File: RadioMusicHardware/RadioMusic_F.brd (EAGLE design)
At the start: 107 x 19.5 mm, 31 parts, among them X1 VERT_SD_CARD_REV2

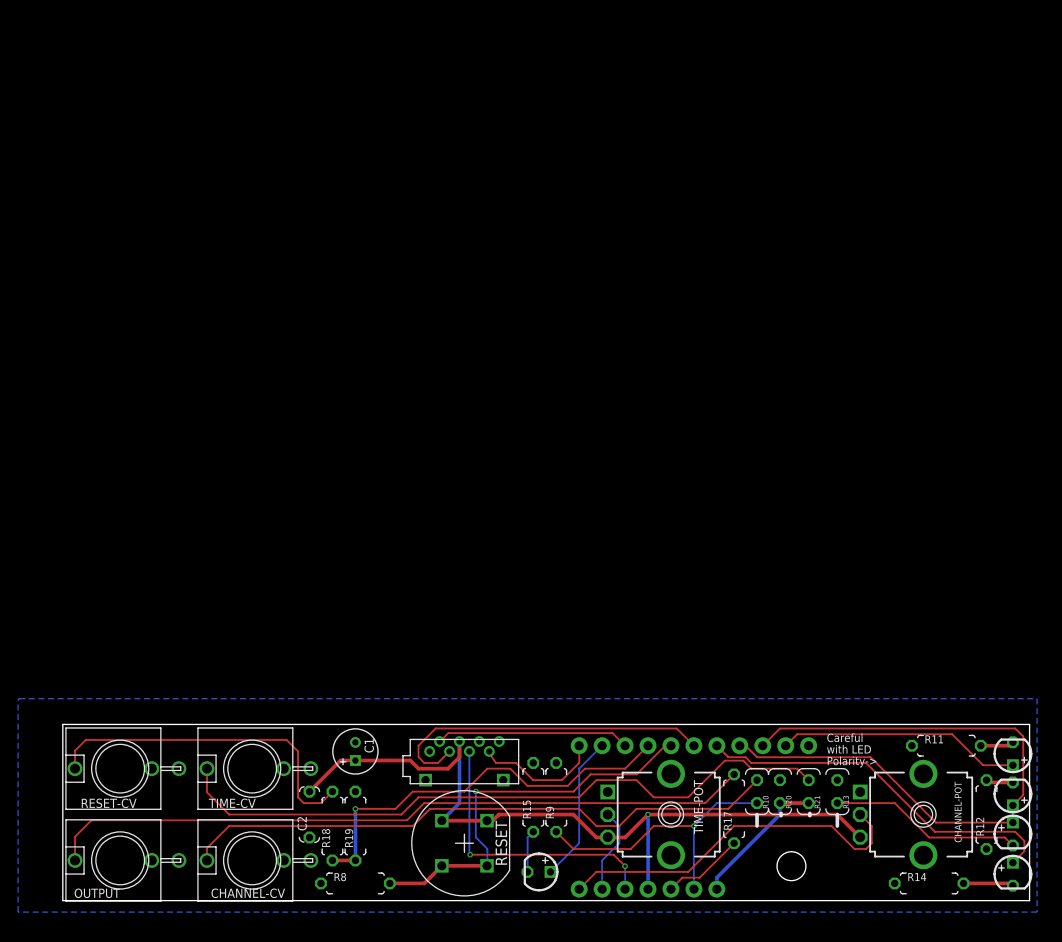
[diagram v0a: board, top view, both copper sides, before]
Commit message: starting SMD needs layout
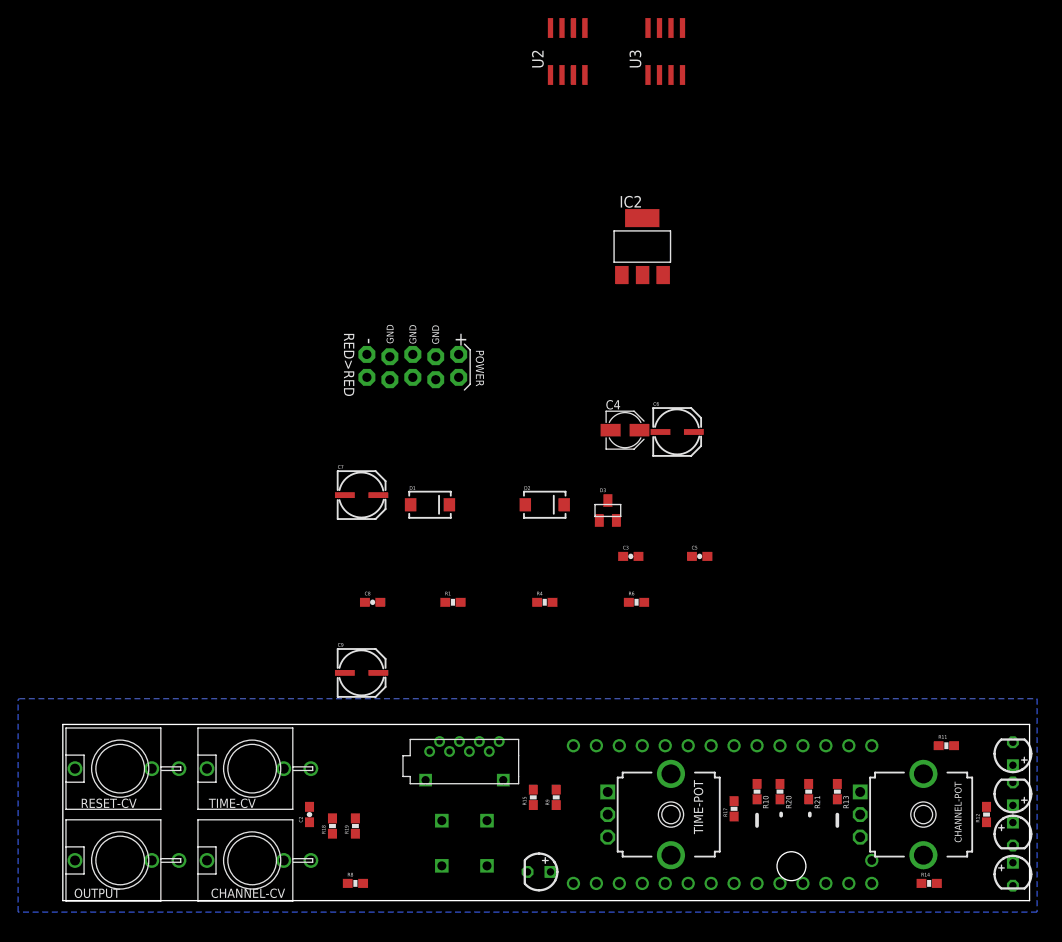
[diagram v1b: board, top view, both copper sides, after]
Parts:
- removed C1: 100uf, gm-caps-electro-pol:050_020
- removed JP2: M11PTH, SparkFun-Connectors:1X11
- removed JP4: (no value), SparkFun-Connectors:1X07
- added C3, C5, C8: 0.1uF, SparkFun-Capacitors:0603-CAP
- added C4: 10uf, rcl:PANASONIC_B
- added C6, C7: 10uf, SparkFun-Passives:PANASONIC_C
- added C9: 100u, SparkFun-Passives:PANASONIC_C
- added D1, D2: DIODE-SCHOTTKY_, SparkFun-DiscreteSemi:SMA-DIODE
- added D3: (no value), SparkFun-DiscreteSemi:SOT23
- added IC2: 5v regulator, burr-brown:SOT223
- added R1, R6: 39k, SparkFun-Passives:0603-RES
- added R4: 5.6k, SparkFun-Passives:0603-RES
- added SV1: EURO_POWER_HEADERLOCK_PADS, MusicThingModular:EURO_PWR_HEADER_LOCK
- added U1: TEENSY_3.1_TW, TomW:TEENSY_3.1_TW
- added U2: MCP6002, MusicThingModular:SO08
- added U3: TL072_SMD, MusicThingModular:SO08
- C2: value 100n -> 0.1uF; device TomW:C050-024X044 -> SparkFun-Capacitors:0603-CAP
- R10, R13, R20, R21: device MusicThingModular:VERTICAL_RESISTOR -> SparkFun-Passives:0603-RES
- R11, R12, R14, R15, R17, R18, R19, R8, R9: device MusicThingModular:7MM_RESISTOR -> SparkFun-Passives:0603-RES
- flipped RESET to the bottom
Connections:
- new net +12V: C5.1, C6.+, D1.C, IC2.3, U3.8
- new net +3.3V: D3.2, U1.3.3V, U2.8
- new net +5V: IC2.2, U1.VIN
- new net -12V: C7.-, C8.2, D2.A, U3.4
- new net AUDIO_OUT: C3.2, R6.2, U3.1
- new net CHANNEL_CV: U2.3
- new net CHANNEL_POT: U1.23/A9
- new net DAC: C4.+, U1.DAC
- new net GND: C5.2, C6.-, C7.+, C8.1, D3.1, IC2.1, SV1.GND1, SV1.GND2, SV1.GND3, SV1.GND4, SV1.GND5, SV1.GND6, U1.AGND, U1.GND, U2.4, U3.3, U3.5
- new net LED1: U1.3
- new net LED2: U1.4
- new net LED3: U1.5
- new net LED4: U1.6
- new net LED_RESET: U1.11
- new net MISO: U1.12
- new net MOSI: U1.7
- new net N$4: C4.-, R1.2, R4.1
- new net N$5: C3.1, R4.2, R6.1, U3.2
- new net N$7: U3.6, U3.7
- new net N$8: D1.A, SV1.POS1, SV1.POS2
- new net N$9: D2.C, SV1.NEG1, SV1.NEG2
- new net PIN20/A6: U1.20/A6, U2.6, U2.7
- new net PIN22/A8: U1.22/A8, U2.1, U2.2
- new net RESET_CV: D3.3, U1.9
- new net RESET_SW: U1.8
- new net SCLK: U1.14/A0
- new net SS: U1.10
- new net TIME_CV: U2.5
- new net TIME_POT: U1.21/A7
- net +3.3V_F: now also C9.+; no longer C1.+, JP4.4
- net AUDIO_OUT_F: no longer JP4.5
- net CHANNEL_CV_F: no longer JP4.6
- net CHANNEL_POT_F: no longer JP4.1
- net GND_F: now also C9.-; no longer C1.-, JP2.1
- net LED1_F: no longer JP2.2
- net LED2_F: no longer JP2.3
- net LED3_F: no longer JP2.4
- net LED4_F: no longer JP2.5
- net LED_RESET_F: no longer JP2.10
- net MISO_F: no longer JP2.11
- net MOSI_F: no longer JP2.6
- net RESET_CV_F: no longer JP2.8
- net RESET_SW_F: no longer JP2.7
- net SCLK_F: no longer JP4.3
- net SS_F: no longer JP2.9
- net TIME_CV_F: no longer JP4.7
- net TIME_POT_F: no longer JP4.2
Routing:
- net +3.3V_F: track 88.4 -> 0.00 mm, vias 1 -> 0
- net N$3: track 78.4 -> 0.00 mm
- net N$2: track 75.2 -> 0.00 mm
- net N$1: track 66.9 -> 0.00 mm
- net RESET_CV_F: track 45.1 -> 0.00 mm, vias 1 -> 0
- net RESET_SW_F: track 44.0 -> 0.00 mm, vias 1 -> 0
- net LED4_F: track 41.3 -> 0.00 mm
- net CHANNEL_POT_F: track 40.3 -> 0.00 mm
- net LED2_F: track 38.1 -> 0.00 mm
- net MOSI_F: track 37.5 -> 0.00 mm
- net N$14: track 37.4 -> 0.00 mm
- net LED3_F: track 33.8 -> 0.00 mm
- net CHANNEL_CV_F: track 32.1 -> 0.00 mm, vias 1 -> 0
- net SCLK_F: track 31.7 -> 0.00 mm, vias 2 -> 0
- net LED1_F: track 27.1 -> 0.00 mm
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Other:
- board text removed: "-->"
- board text removed: "Careful with LED Polarity->"

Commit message: everything fits on the board, but not properly placed or routed
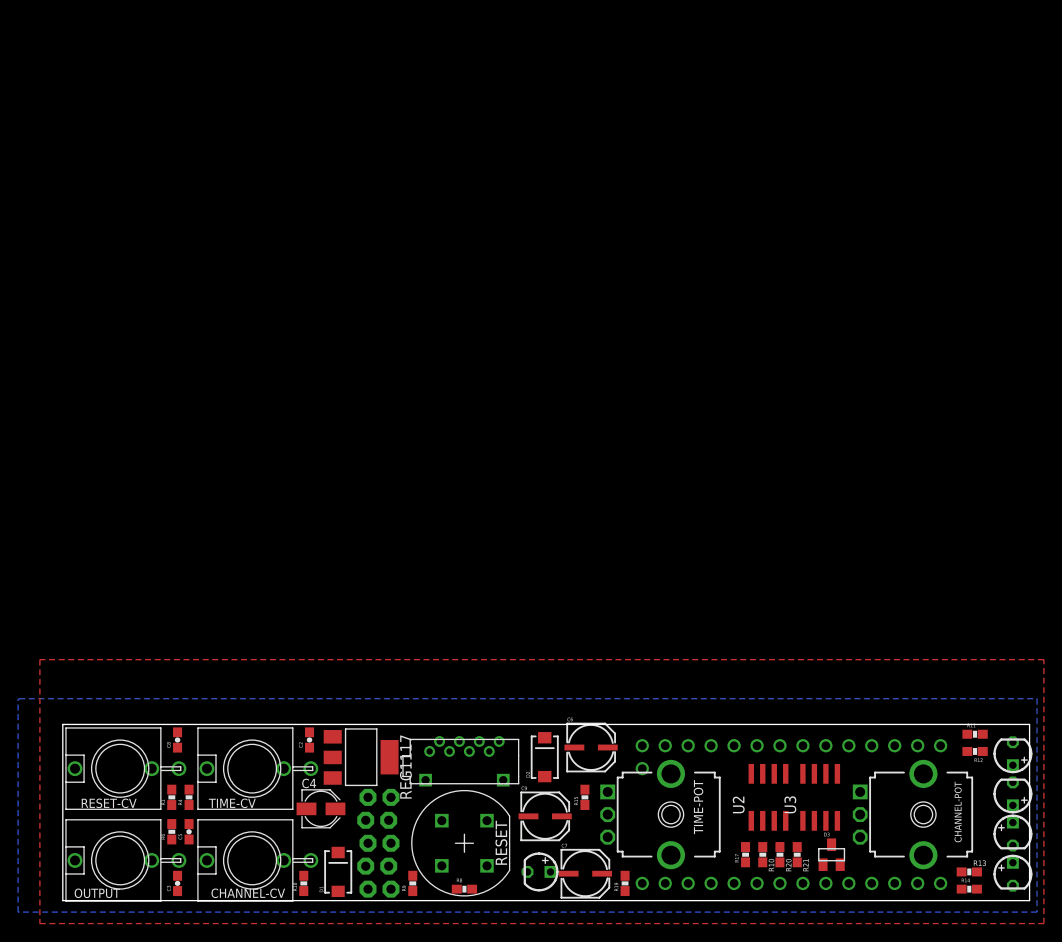
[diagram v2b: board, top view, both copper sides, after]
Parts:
- removed IC2: 5v regulator, burr-brown:SOT223
- removed U$2: (no value), MusicThingModular:MOUNTING_HOLE
- added REG1117: 5v regulator, burr-brown:SOT223
- moved U2 85.5 mm to (78.1, 11.4)
- moved U3 84.3 mm to (83.8, 11.4)
- moved C5 64.2 mm to (14.0, 7.62), turned to 90 degrees
- moved C3 61.9 mm to (12.7, 1.91), turned to 90 degrees
- moved R6 57.4 mm to (12.1, 7.62), turned to 90 degrees
- moved C4 53.8 mm to (28.6, 10.2)
- moved SV1 52.8 mm to (34.9, 6.35), flipped to the bottom, turned to 90 degrees
- moved C7 48.7 mm to (57.8, 3.17)
- moved D3 45.4 mm to (85.1, 5.08)
- moved R4 44.9 mm to (14.0, 11.4), turned to 90 degrees
- moved D1 41.9 mm to (30.5, 3.17), turned to 90 degrees
- moved R1 37.9 mm to (12.1, 11.4), turned to 90 degrees
- moved C6 36.2 mm to (58.4, 17.1)
- moved R19 30.5 mm to (62.2, 1.91)
- moved D2 27.9 mm to (53.3, 15.9), turned to 90 degrees
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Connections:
- net +12V: now also REG1117.3; no longer IC2.3
- net +5V: now also REG1117.2; no longer IC2.2
- net GND: now also REG1117.1; no longer IC2.1
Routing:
- added copper zone on layer 1, net GND
